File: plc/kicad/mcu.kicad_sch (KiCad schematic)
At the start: 61 parts, among them J2 Conn_01x04_Pin, Q3 L8050QLT1G, Q4 L8050QLT1G, SW1 TSD003B08026A03, SW2 TSD003B08026A03, U10 ESP32-S3-MINI-1U, U11 BS-0601-SK-4W, U12 AHT20_C2757850, U13 CP2102N-A02-GQFN28R, U9 RV-3028-C7

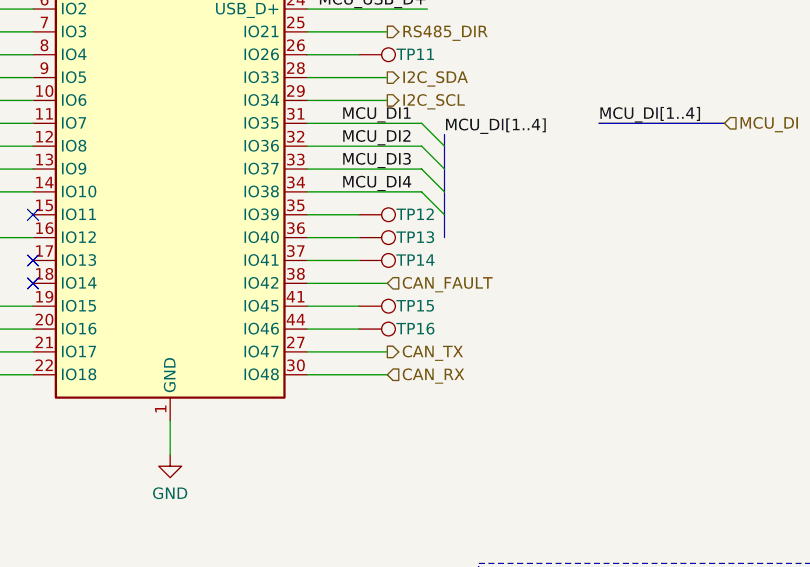
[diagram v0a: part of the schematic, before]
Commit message: Added isolated CAN bus
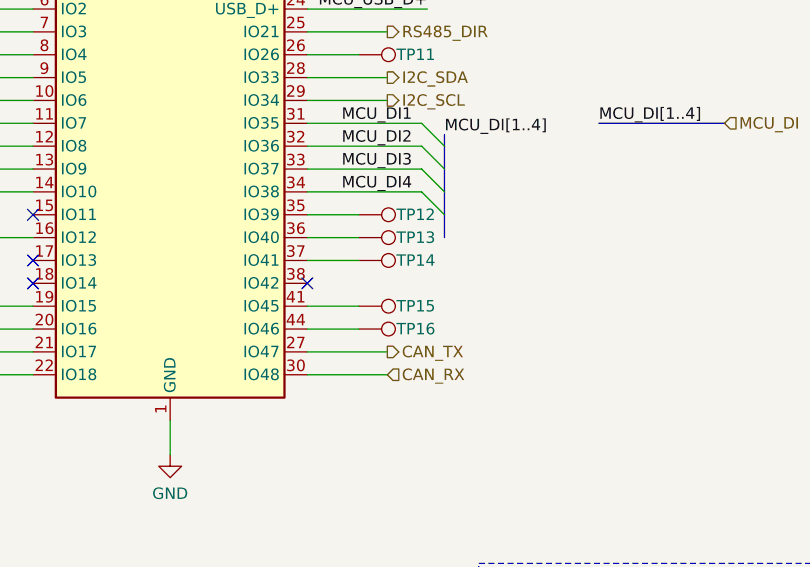
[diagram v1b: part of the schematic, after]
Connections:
- net CAN_FAULT: no longer names the net of U10.38 (IO42)
- no-connect marks 26 -> 27
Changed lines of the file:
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@@
+	)
+	(no_connect
+		(at 125.73 90.17)
 	)
 	(no_connect
@@
 	(wire
 		(pts
-			(xy 134.62 90.17) (xy 125.73 90.17)
-		)
-		(stroke
-			(width 0)
-			(type default)
-		)
-	)
-	(wire
-		(pts
 			(xy 247.269 92.964) (xy 252.349 92.964)
 		)
@@
 		)
 	)
-	(hierarchical_label "CAN_FAULT"
-		(shape input)
-		(at 134.62 90.17 0)
-		(effects
-			(font
-				(size 1.27 1.27)
-			)
-			(justify left)
-		)
-	)

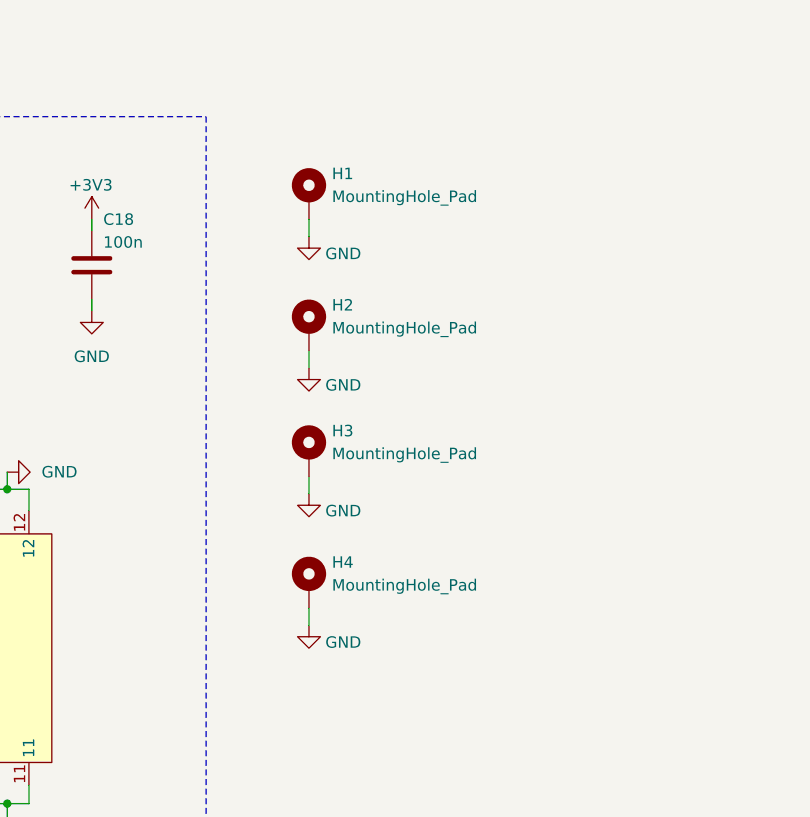
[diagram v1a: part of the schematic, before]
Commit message: Added more mounting holes
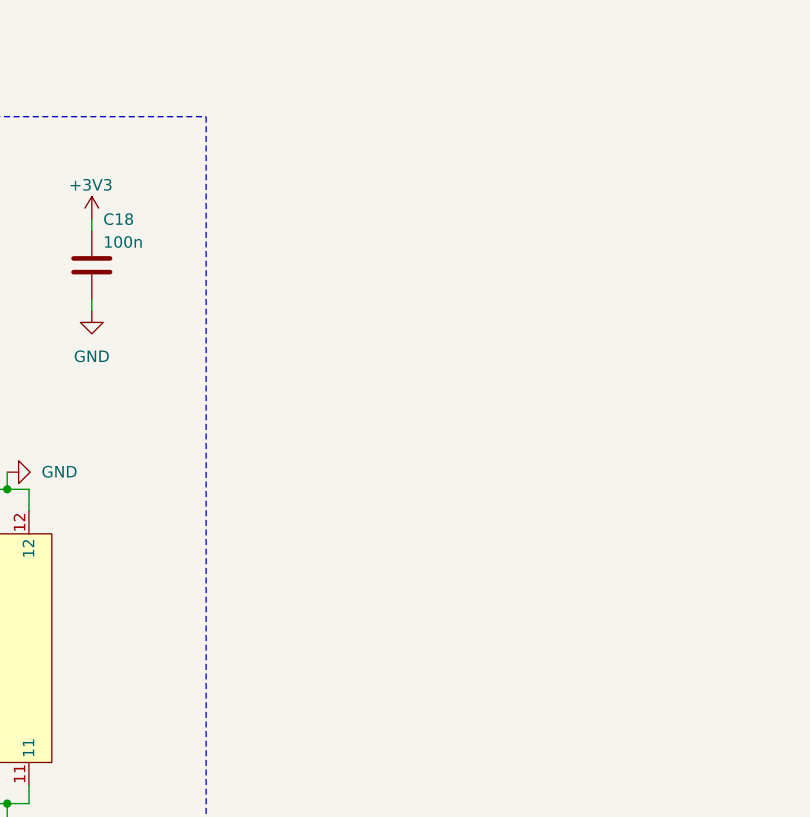
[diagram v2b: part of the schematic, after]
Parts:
- removed H1, H2, H3, H4: MountingHole_Pad, MountingHole:MountingHole_4.3mm_M4_DIN965_Pad_TopBottom, symbol Mechanical:MountingHole_Pad

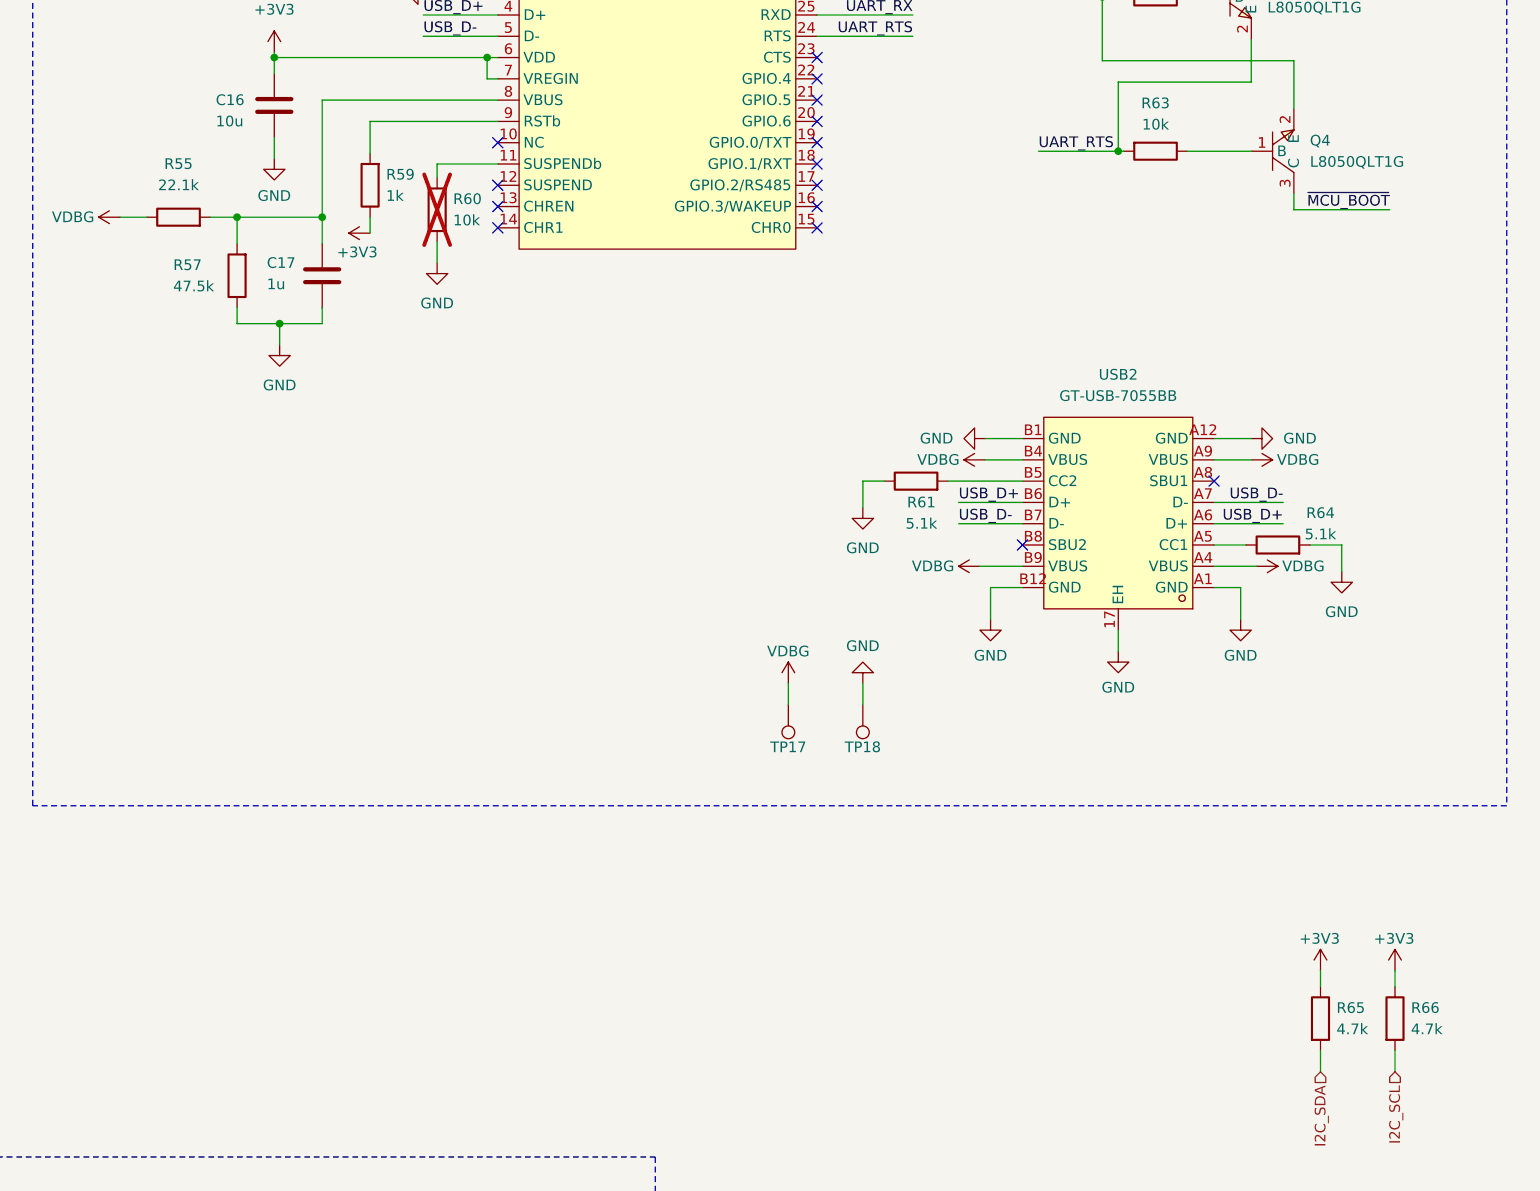
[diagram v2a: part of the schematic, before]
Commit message: BOM Consolidation
- CP2102N Vdbg divider: 22.1k→5.1k, 47.5k→10k (gives 3.29V)
- I²C pull-ups (R65,R66): 4.7k→5.1k (verified ok)
- Buck UVLO (R69,R70): 442k→100k, 90.9k→2×10k (UVLO = 7V)
- TPS272C45D ILIM (R75): 3k→3×10k (~6A limit)
- PPIC IMON + ETH_EXPRESS (R77,R100): 12.4k→2×6.2k
- Buck compensation (R78): 16.9k→10k+6.2k+620 series
- PPIC PGTH divider (R79,R80): 499k→100k, 55.44k→2×10k (PGTH = 7.2V)
- Buck feedback (R82,R83): 53.6k→52.5k 1%, 10.2k→10k 1%
- 3.3V LDO power-good (R88): 50k→100k

| Metric                 | Before | After | Change             |
| ---------------------- | ------ | ----- | ------------------ |
| Unique resistor values | 33     | 22    | **−11 (−33%)**     |
| Total resistor count   | 110    | 118   | +8 (series splits) |
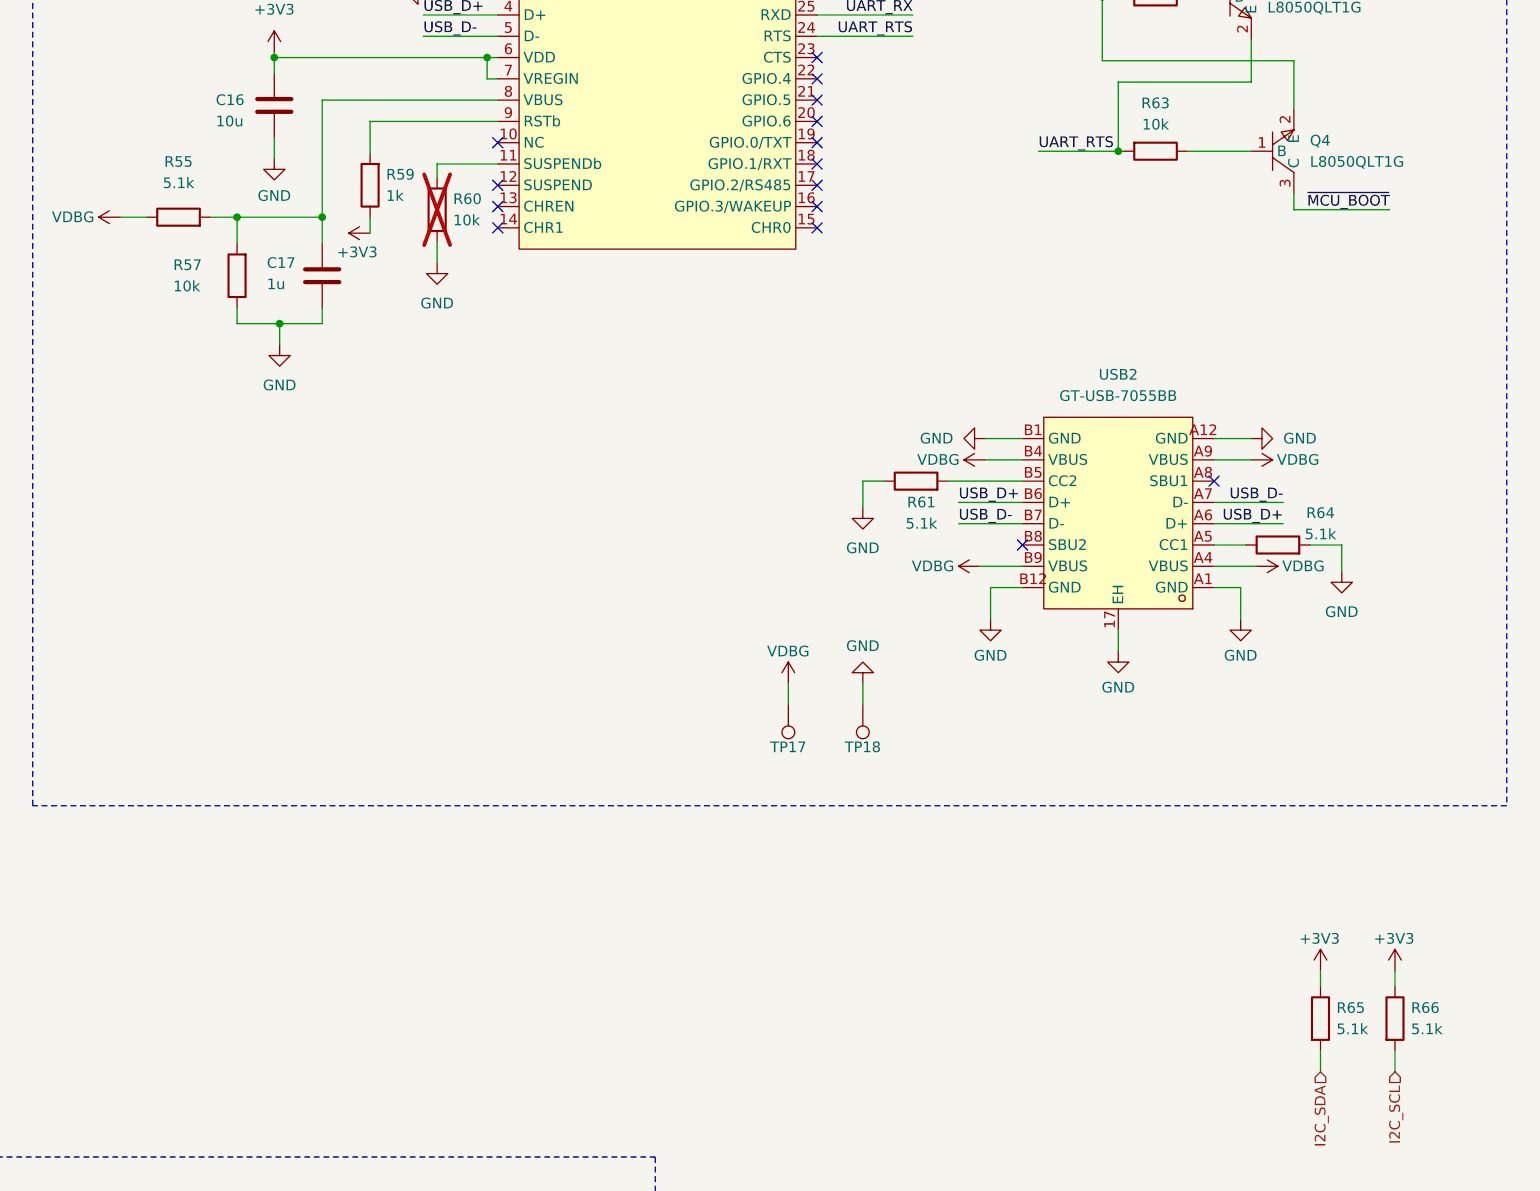
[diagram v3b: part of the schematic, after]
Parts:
- R55: value 22.1k -> 5.1k
- R57: value 47.5k -> 10k
- R65, R66: value 4.7k -> 5.1k
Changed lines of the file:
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@@
 			)
 		)
-		(property "Value" "4.7k"
+		(property "Value" "5.1k"
 			(at 378.46 177.1649 0)
 			(show_name no)
@@
 			)
 		)
-		(property "Value" "47.5k"
+		(property "Value" "10k"
 			(at 239.649 88.519 0)
 			(show_name no)
@@
 			)
 		)
-		(property "Value" "4.7k"
+		(property "Value" "5.1k"
 			(at 387.35 177.1649 0)
 			(show_name no)
@@
 		(fields_autoplaced yes)
 		(property "Reference" "R55"
-			(at 240.284 73.914 90)
+			(at 240.284 73.66 90)
 			(show_name no)
 			(do_not_autoplace no)
@@
 			)
 		)
-		(property "Value" "22.1k"
-			(at 240.284 76.454 90)
+		(property "Value" "5.1k"
+			(at 240.284 76.2 90)
 			(show_name no)
 			(do_not_autoplace no)
